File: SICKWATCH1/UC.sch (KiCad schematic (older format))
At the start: 25 parts, among them SW1 SW_Push, U1 STM32F103C8Tx, Y1 Crystal

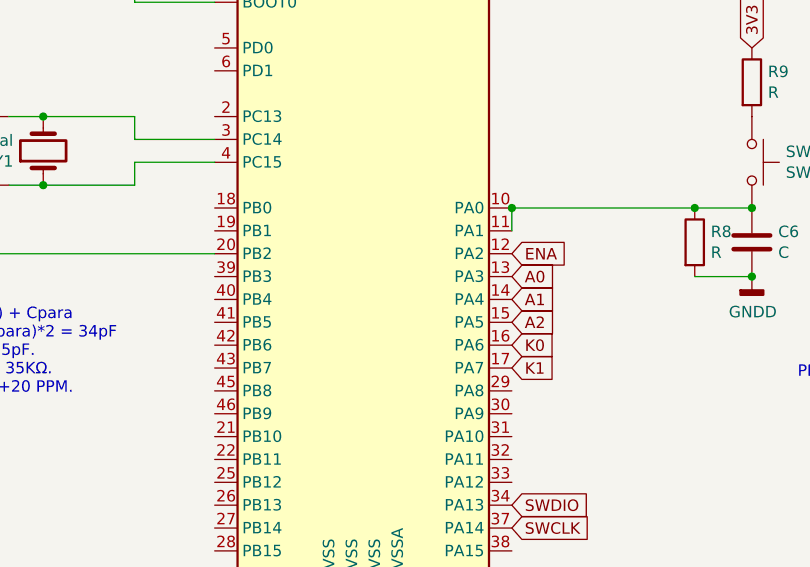
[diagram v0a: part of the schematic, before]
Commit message: fixed screenprints
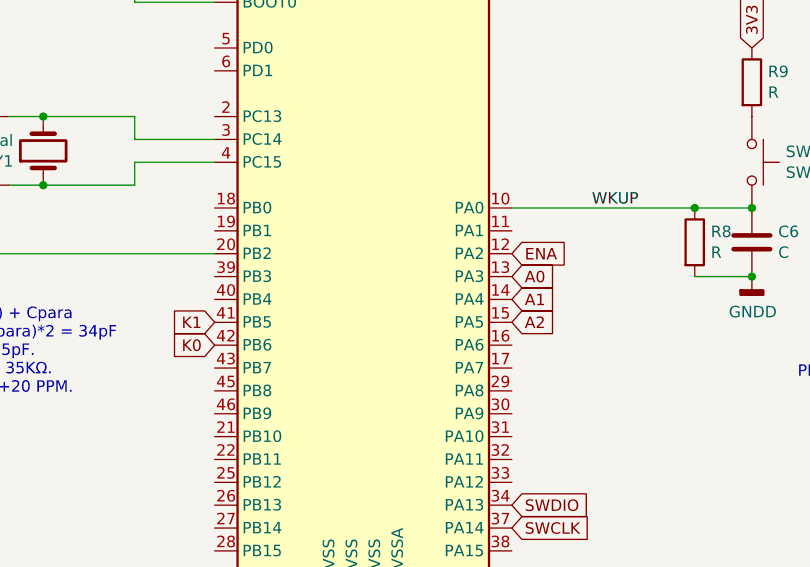
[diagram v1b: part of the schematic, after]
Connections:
- net K0: now also U1.42 (PB6); no longer U1.16 (PA6)
- net K1: now also U1.41 (PB5); no longer U1.17 (PA7)
- net WKUP: now reaches C6.1, R8.1, SW1.2, U1.10 (PA0)
- net WKUP: no longer U1.11 (PA1)
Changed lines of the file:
@@
 $EndComp
 Connection ~ 7700 3400
-Wire Wire Line
-	6650 3500 6650 3400
 $Comp
 L Device:R R7
@@
 Text Notes 3650 4300 0    50   ~ 0
 LOAD Capacitance: \nCL = (C1*C2)/(C1+C2) + Cpara\nC = C1 = C2 = (CL -Cpara)*2 = 34pF\nLoad Capacitance: 12.5pF.\nEquivalent resistance: 35KΩ.\nFrequency tolerance: +20 PPM.\n32738
-Text GLabel 6650 4100 2    50   Input ~ 0
+Text GLabel 5350 3900 0    50   Input ~ 0
 K1
 Wire Wire Line
@@
 Connection ~ 6050 2100
 Connection ~ 5950 2100
-Text GLabel 6650 4000 2    50   Input ~ 0
+Text GLabel 5350 4000 0    50   Input ~ 0
 K0
 Text GLabel 6650 3600 2    50   Input ~ 0
@@
 Wire Wire Line
 	5000 2500 5000 1900
-Connection ~ 6650 3400
 Connection ~ 7450 3400
 Connection ~ 7700 3700
@@
 Text GLabel 6650 4800 2    50   Input ~ 0
 SWCLK
+Text Label 7000 3400 0    50   ~ 0
+WKUP
 $EndSCHEMATC
